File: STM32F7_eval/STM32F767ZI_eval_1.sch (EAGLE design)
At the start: 101 parts, among them CN3 GROVE-4P-CONN-I2C-90D, CN4 GROVE-4P-CONN-I2C-90D, CN5 ARDUINO_COMPAT_IF, CN6 STLINKV21_SWD_IF, CN7 WFT0750CZ09-SMD_, CN9 UART_IF, Q1 PMF370XN_, SW1 SKRPACE010_, SW2 SKRPACE010_, U1 STM32F767ZI_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

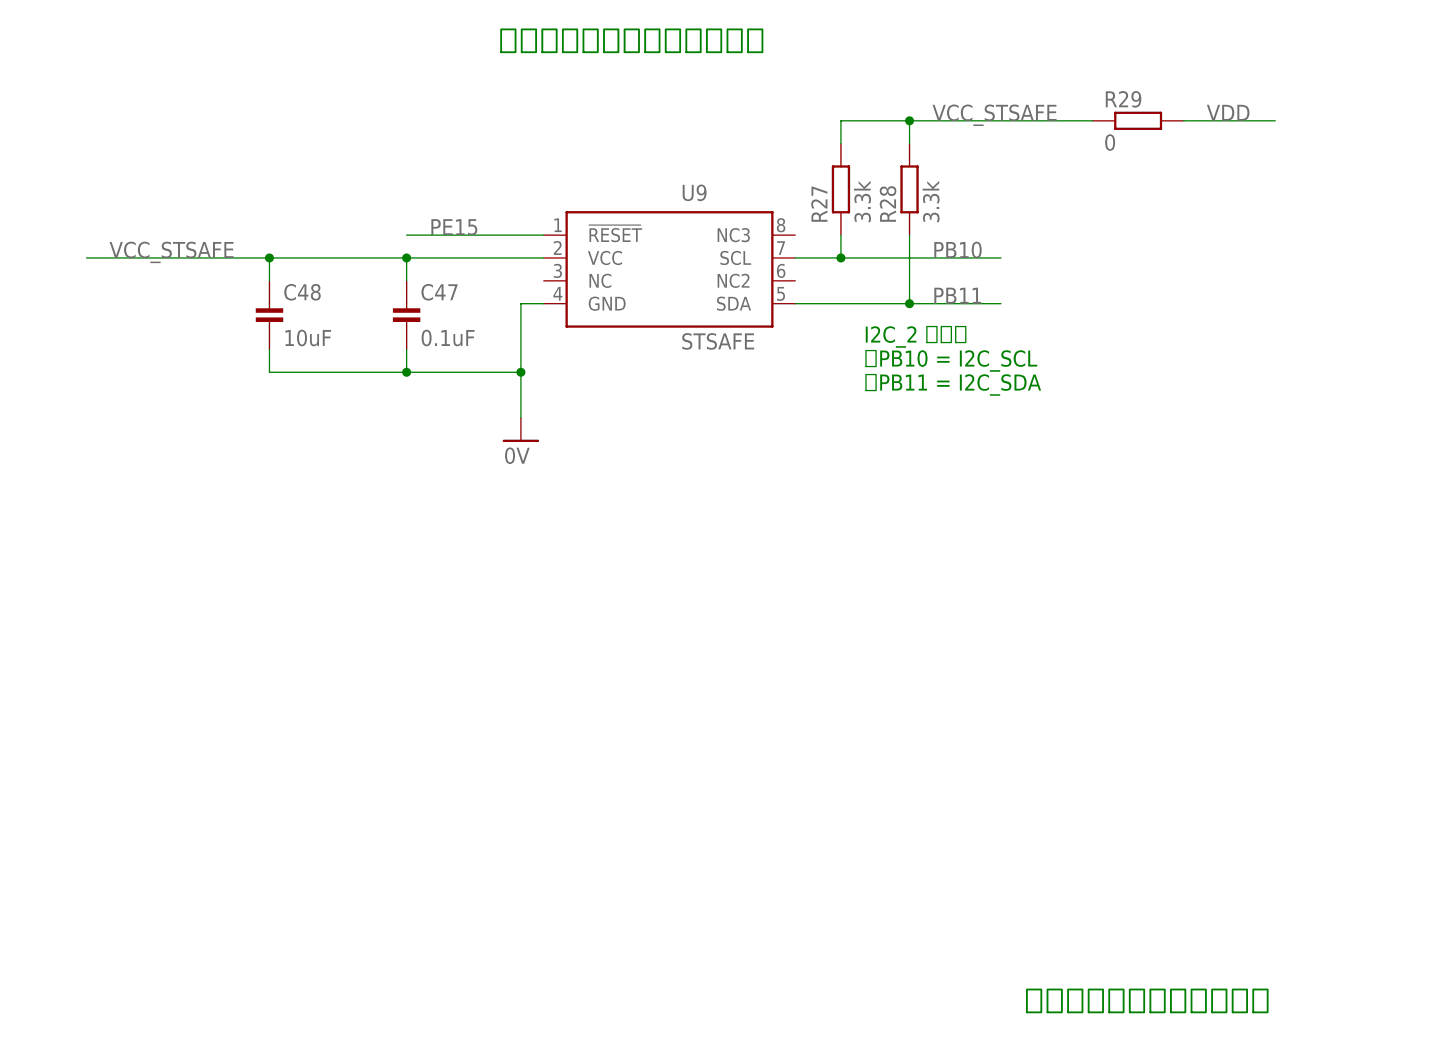
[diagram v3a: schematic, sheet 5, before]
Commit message: 回路図を修正
・回路図のレイアウトを修正
・定数変更
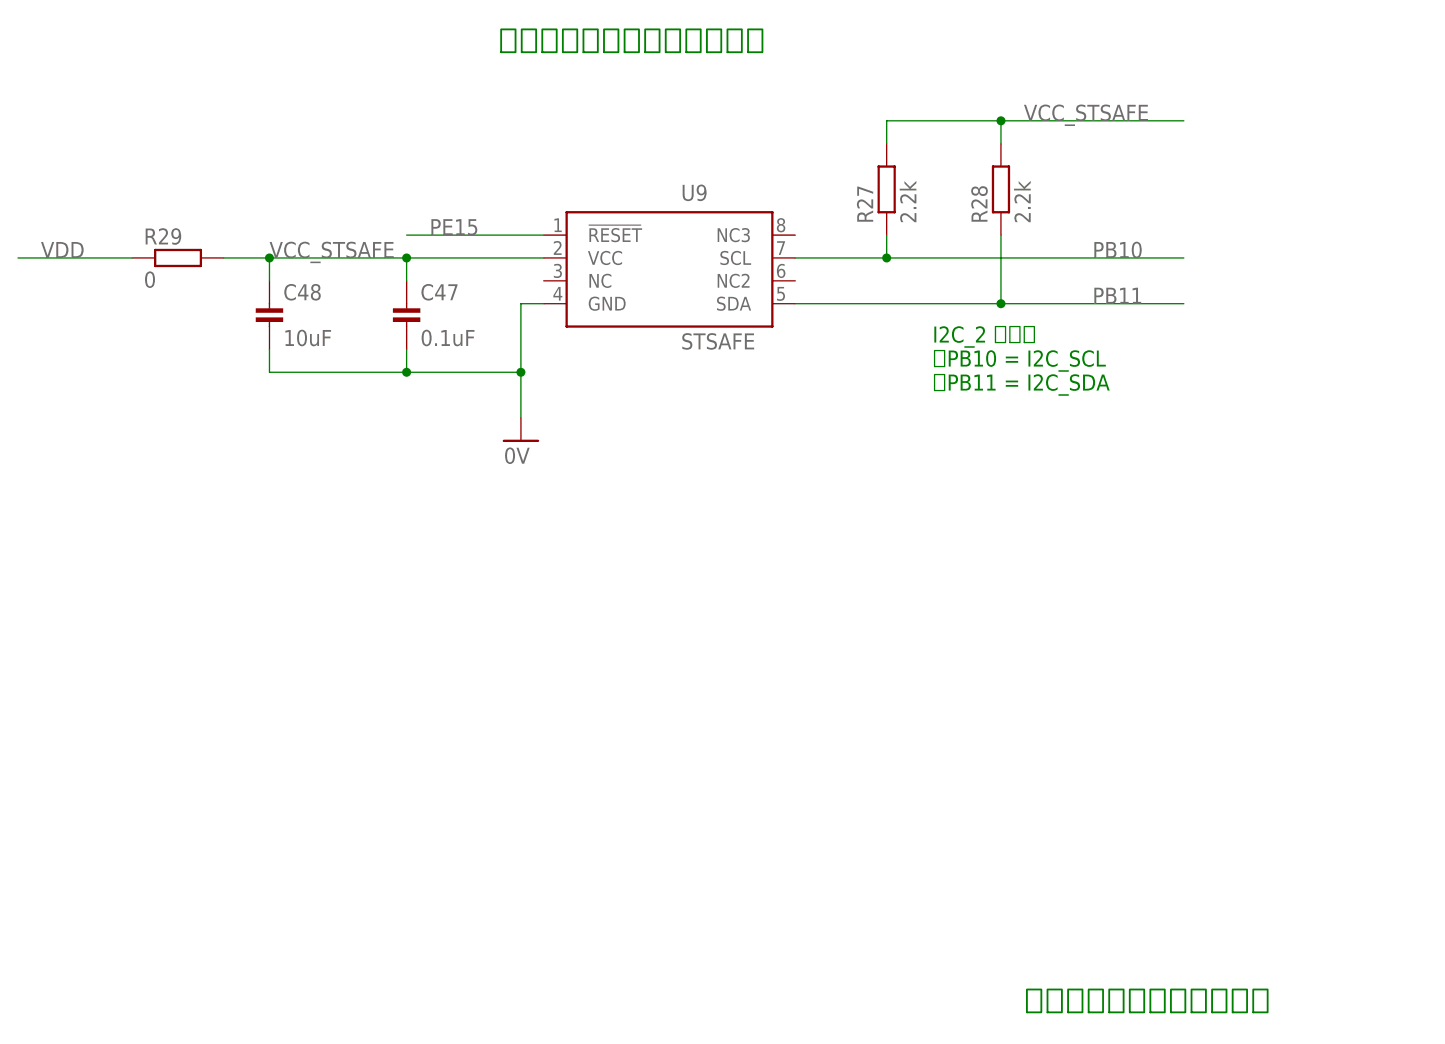
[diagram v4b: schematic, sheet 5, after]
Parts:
- R27, R28: value 3.3k -> 2.2k
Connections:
- net VCC_STSAFE: now also R29.2; no longer R29.1
- net VDD: now also R29.1; no longer R29.2
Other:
- moved on the sheet: R27, R28, R29
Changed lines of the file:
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@@
 <part name="C47" library="Parts" deviceset="CAP" device="_0603_DEV" value="0.1uF"/>
 <part name="C48" library="Parts" deviceset="CAP" device="_0805_DEV" value="10uF"/>
-<part name="R27" library="Parts" deviceset="RESISTOR" device="_0603_DEV" value="3.3k"/>
-<part name="R28" library="Parts" deviceset="RESISTOR" device="_0603_DEV" value="3.3k"/>
+<part name="R27" library="Parts" deviceset="RESISTOR" device="_0603_DEV" value="2.2k"/>
+<part name="R28" library="Parts" deviceset="RESISTOR" device="_0603_DEV" value="2.2k"/>
 <part name="U9" library="Parts" deviceset="STSAFE" device=""/>
 <part name="GND22" library="Supply" deviceset="0V" device=""/>
@@
 <text x="167.64" y="12.7" size="2.54" layer="91">オプションデバイス配線図</text>
 <text x="109.22" y="119.38" size="2.54" layer="91">セキュリティーチップ回路図</text>
-<text x="149.86" y="88.9" size="1.778" layer="91" align="top-left">I2C_2 を使用
+<text x="157.48" y="88.9" size="1.778" layer="91" align="top-left">I2C_2 を使用
 ・PB10 = I2C_SCL
 ・PB11 = I2C_SDA
@@
 <instance part="C47" gate="G$1" x="99.06" y="93.98"/>
 <instance part="C48" gate="G$1" x="83.82" y="93.98"/>
-<instance part="R27" gate="G$1" x="147.32" y="99.06" rot="R90"/>
-<instance part="R28" gate="G$1" x="154.94" y="99.06" rot="R90"/>
+<instance part="R27" gate="G$1" x="152.4" y="99.06" rot="R90"/>
+<instance part="R28" gate="G$1" x="165.1" y="99.06" rot="R90"/>
 <instance part="U9" gate="G$1" x="114.3" y="99.06"/>
 <instance part="GND22" gate="1" x="111.76" y="76.2"/>
-<instance part="R29" gate="G$1" x="175.26" y="111.76"/>
+<instance part="R29" gate="G$1" x="68.58" y="96.52"/>
 </instances>
 <busses>
@@
 <segment>
 <pinref part="R27" gate="G$1" pin="1"/>
-<wire x1="142.24" y1="96.52" x2="147.32" y2="96.52" width="0.1524" layer="91"/>
-<wire x1="147.32" y1="96.52" x2="147.32" y2="99.06" width="0.1524" layer="91"/>
-<wire x1="147.32" y1="96.52" x2="165.1" y2="96.52" width="0.1524" layer="91"/>
-<junction x="147.32" y="96.52"/>
-<label x="157.48" y="96.52" size="1.778" layer="95"/>
+<wire x1="142.24" y1="96.52" x2="152.4" y2="96.52" width="0.1524" layer="91"/>
+<wire x1="152.4" y1="96.52" x2="152.4" y2="99.06" width="0.1524" layer="91"/>
+<wire x1="152.4" y1="96.52" x2="185.42" y2="96.52" width="0.1524" layer="91"/>
+<junction x="152.4" y="96.52"/>
+<label x="175.26" y="96.52" size="1.778" layer="95"/>
 <pinref part="U9" gate="G$1" pin="SCL"/>
 </segment>
@@
 <segment>
 <pinref part="R28" gate="G$1" pin="1"/>
-<wire x1="142.24" y1="91.44" x2="154.94" y2="91.44" width="0.1524" layer="91"/>
-<wire x1="154.94" y1="91.44" x2="154.94" y2="99.06" width="0.1524" layer="91"/>
-<wire x1="154.94" y1="91.44" x2="165.1" y2="91.44" width="0.1524" layer="91"/>
-<junction x="154.94" y="91.44"/>
-<label x="157.48" y="91.44" size="1.778" layer="95"/>
+<wire x1="142.24" y1="91.44" x2="165.1" y2="91.44" width="0.1524" layer="91"/>
+<wire x1="165.1" y1="91.44" x2="165.1" y2="99.06" width="0.1524" layer="91"/>
+<wire x1="165.1" y1="91.44" x2="185.42" y2="91.44" width="0.1524" layer="91"/>
+<junction x="165.1" y="91.44"/>
+<label x="175.26" y="91.44" size="1.778" layer="95"/>
 <pinref part="U9" gate="G$1" pin="SDA"/>
 </segment>
@@
 <segment>
 <pinref part="R27" gate="G$1" pin="2"/>
-<wire x1="147.32" y1="109.22" x2="147.32" y2="111.76" width="0.1524" layer="91"/>
-<wire x1="147.32" y1="111.76" x2="154.94" y2="111.76" width="0.1524" layer="91"/>
+<wire x1="152.4" y1="109.22" x2="152.4" y2="111.76" width="0.1524" layer="91"/>
+<wire x1="152.4" y1="111.76" x2="165.1" y2="111.76" width="0.1524" layer="91"/>
 <pinref part="R28" gate="G$1" pin="2"/>
-<wire x1="154.94" y1="111.76" x2="175.26" y2="111.76" width="0.1524" layer="91"/>
-<wire x1="154.94" y1="109.22" x2="154.94" y2="111.76" width="0.1524" layer="91"/>
-<junction x="154.94" y="111.76"/>
-<label x="157.48" y="111.76" size="1.778" layer="95"/>
-<pinref part="R29" gate="G$1" pin="1"/>
+<wire x1="165.1" y1="109.22" x2="165.1" y2="111.76" width="0.1524" layer="91"/>
+<label x="167.64" y="111.76" size="1.778" layer="95"/>
+<wire x1="165.1" y1="111.76" x2="185.42" y2="111.76" width="0.1524" layer="91"/>
+<junction x="165.1" y="111.76"/>
 </segment>
 <segment>
@@
 <pinref part="C48" gate="G$1" pin="1"/>
 <wire x1="99.06" y1="96.52" x2="83.82" y2="96.52" width="0.1524" layer="91"/>
-<wire x1="83.82" y1="96.52" x2="63.5" y2="96.52" width="0.1524" layer="91"/>
 <wire x1="83.82" y1="93.98" x2="83.82" y2="96.52" width="0.1524" layer="91"/>
-<junction x="83.82" y="96.52"/>
 <pinref part="C47" gate="G$1" pin="1"/>
 <wire x1="99.06" y1="93.98" x2="99.06" y2="96.52" width="0.1524" layer="91"/>
 <junction x="99.06" y="96.52"/>
-<label x="66.04" y="96.52" size="1.778" layer="95"/>
-</segment>
-</net>
-<net name="VDD" class="0">
-<segment>
+<label x="83.82" y="96.52" size="1.778" layer="95"/>
 <pinref part="R29" gate="G$1" pin="2"/>
-<wire x1="185.42" y1="111.76" x2="195.58" y2="111.76" width="0.1524" layer="91"/>
-<label x="187.96" y="111.76" size="1.778" layer="95"/>
+<wire x1="83.82" y1="96.52" x2="78.74" y2="96.52" width="0.1524" layer="91"/>
+<junction x="83.82" y="96.52"/>
 </segment>
 </net>
@@
 </segment>
 </net>
+<net name="VDD" class="0">
+<segment>
+<pinref part="R29" gate="G$1" pin="1"/>
+<wire x1="68.58" y1="96.52" x2="55.88" y2="96.52" width="0.1524" layer="91"/>
+<label x="58.42" y="96.52" size="1.778" layer="95"/>
+</segment>
+</net>

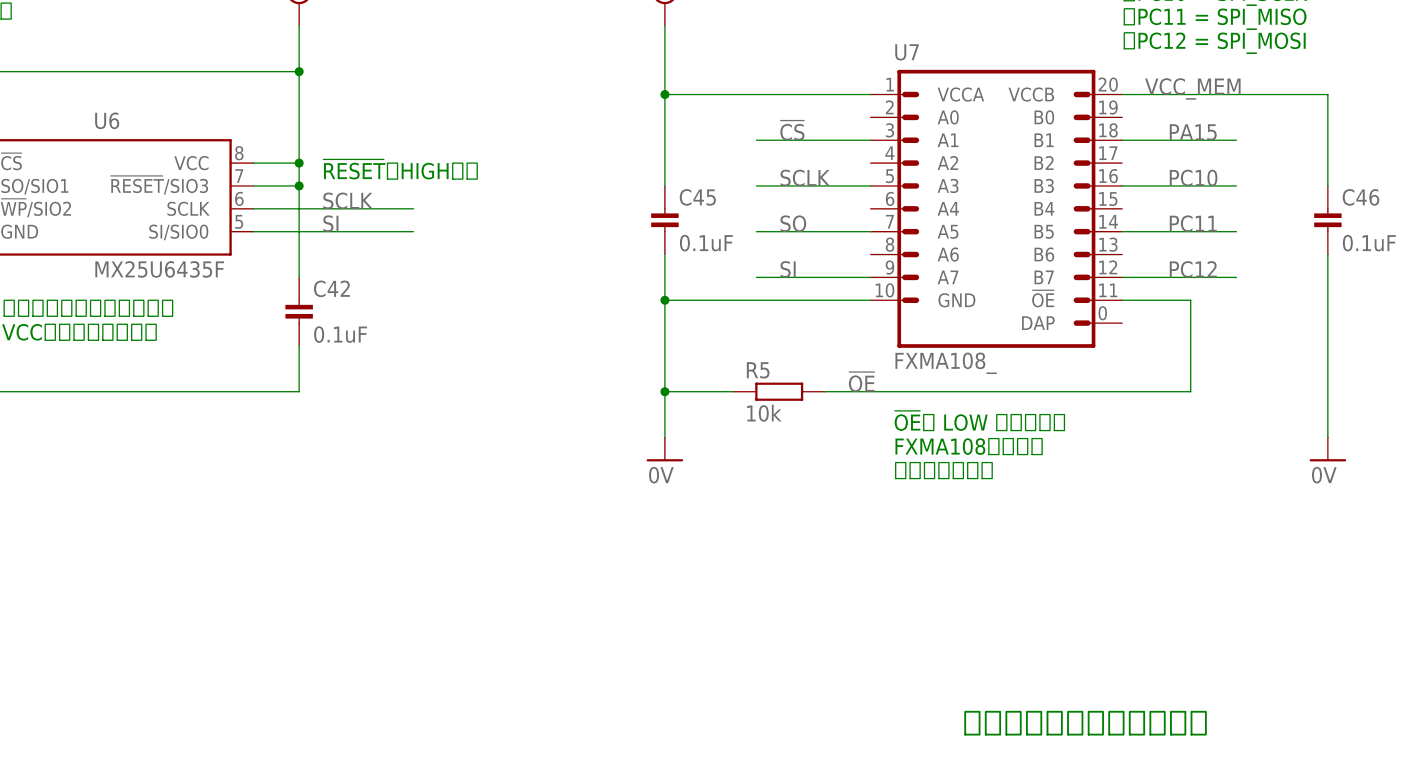
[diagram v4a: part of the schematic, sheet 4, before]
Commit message: 回路図を修正
・回路図のレイアウトを修正
・ダンピング抵抗追加
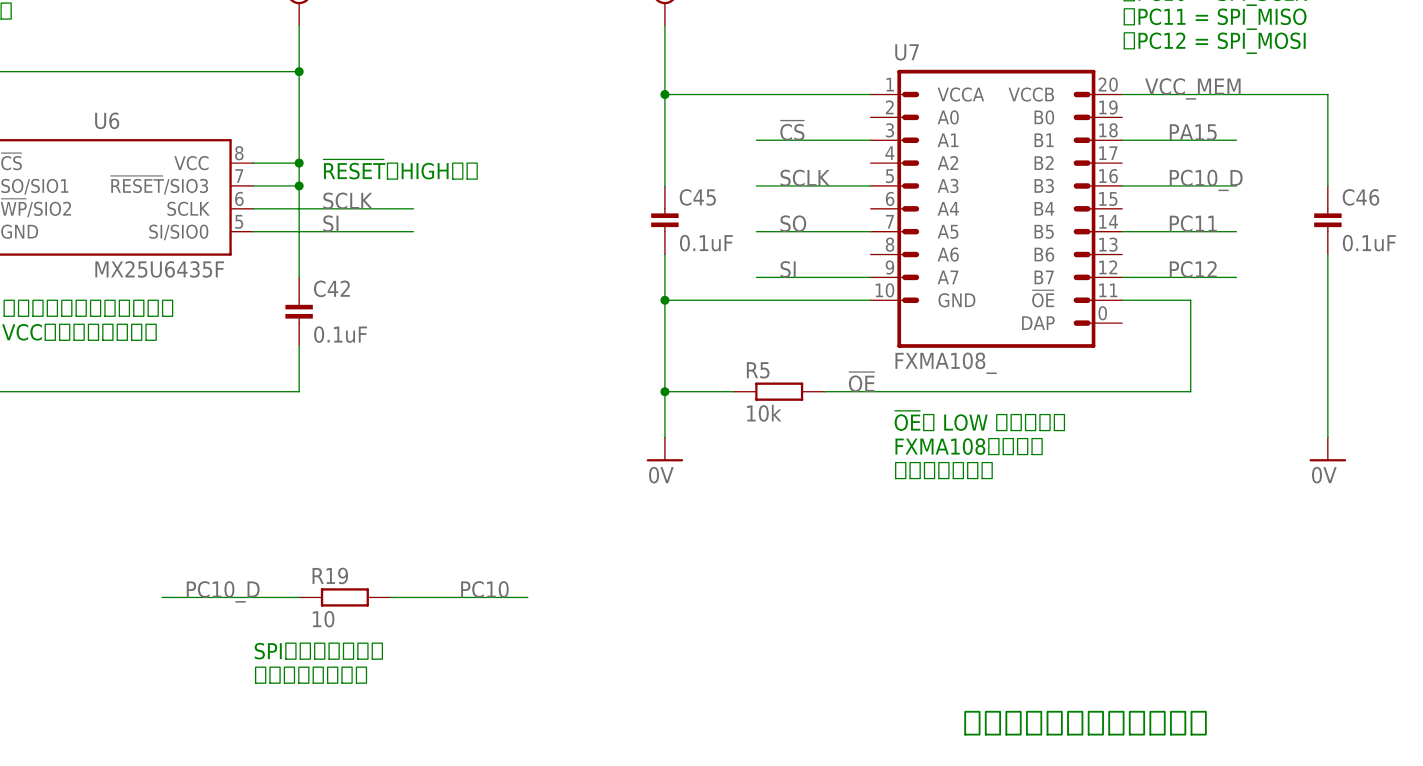
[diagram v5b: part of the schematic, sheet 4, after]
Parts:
- added R19: 10, Parts:RESISTOR_0603_DEV
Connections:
- new net PC10_D: R19.1, U7.B3
- net PC10: now also R19.2; no longer U7.B3
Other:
- note added: "SPIクロック信号の ダンピング用抵抗"
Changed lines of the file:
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@@
 <part name="C49" library="Parts" deviceset="CAP" device="_0603_DEV" value="1uF X5R"/>
 <part name="GND13" library="Supply" deviceset="0V" device=""/>
+<part name="R19" library="Parts" deviceset="RESISTOR" device="_0603_DEV" value="10"/>
 </parts>
 <sheets>
@@
 <text x="147.32" y="119.38" size="1.778" layer="91" align="top-left">1uFはVOUTピンの
 近傍に設置</text>
+<text x="88.9" y="22.86" size="1.778" layer="91" align="top-left">SPIクロック信号の
+ダンピング用抵抗</text>
 </plain>
 <instances>
@@
 <instance part="C49" gate="G$1" x="91.44" y="134.62"/>
 <instance part="GND13" gate="1" x="208.28" y="43.18"/>
+<instance part="R19" gate="G$1" x="93.98" y="27.94"/>
 </instances>
 <busses>
@@
 </segment>
 </net>
-<net name="PC10" class="0">
-<segment>
-<pinref part="U7" gate="G$1" pin="B3"/>
-<wire x1="185.42" y1="73.66" x2="198.12" y2="73.66" width="0.1524" layer="91"/>
-<label x="190.5" y="73.66" size="1.778" layer="95"/>
-</segment>
-</net>
 <net name="+1V8" class="0">
 <segment>
@@
 </segment>
 </net>
+<net name="PC10" class="0">
+<segment>
+<pinref part="R19" gate="G$1" pin="2"/>
+<wire x1="104.14" y1="27.94" x2="119.38" y2="27.94" width="0.1524" layer="91"/>
+<label x="111.76" y="27.94" size="1.778" layer="95"/>
+</segment>
+</net>
+<net name="PC10_D" class="0">
+<segment>
+<pinref part="R19" gate="G$1" pin="1"/>
+<wire x1="93.98" y1="27.94" x2="78.74" y2="27.94" width="0.1524" layer="91"/>
+<label x="81.28" y="27.94" size="1.778" layer="95"/>
+</segment>
+<segment>
+<pinref part="U7" gate="G$1" pin="B3"/>
+<wire x1="185.42" y1="73.66" x2="198.12" y2="73.66" width="0.1524" layer="91"/>
+<label x="190.5" y="73.66" size="1.778" layer="95"/>
+</segment>
+</net>
